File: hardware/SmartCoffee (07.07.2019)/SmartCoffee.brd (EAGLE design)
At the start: 96 x 40 mm, 32 parts, among them IC1 ULN2003V12DR, K1 G2R

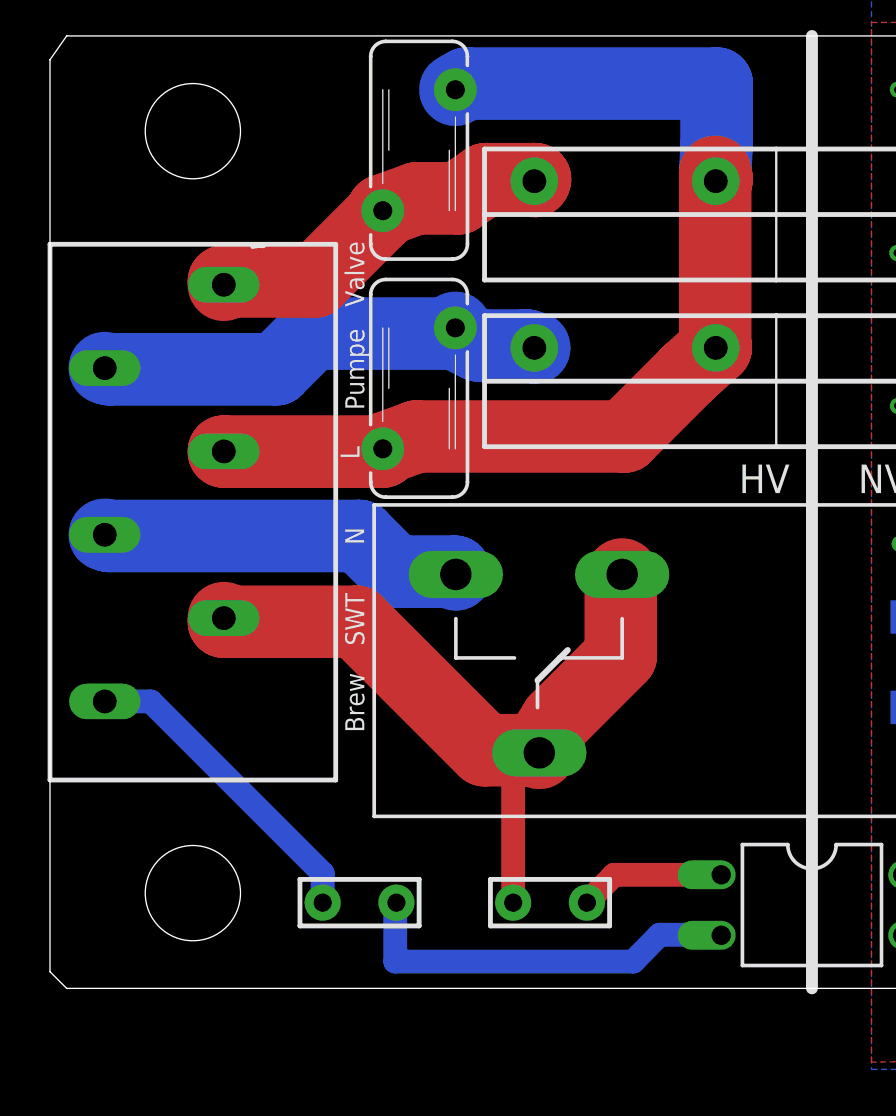
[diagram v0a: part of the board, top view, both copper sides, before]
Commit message: 
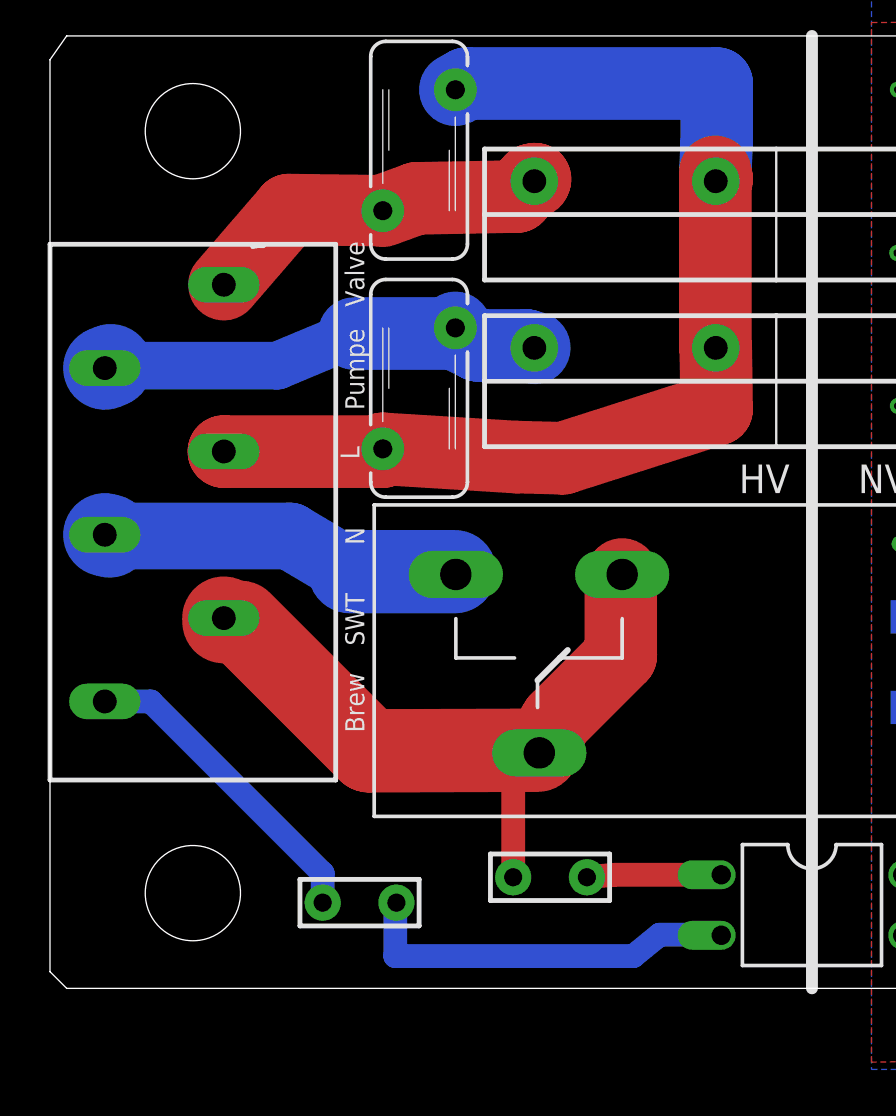
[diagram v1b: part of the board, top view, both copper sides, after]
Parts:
- moved R4 1.07 mm to (21.0, 4.67)
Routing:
- net HV_L: track 45.7 -> 47.0 mm
- net HV_N_SWITCHED: track 31.8 -> 30.8 mm
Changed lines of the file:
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@@
 <attribute name="VALUE" x="67.6506" y="39.3556" size="0.6" layer="122" font="vector" rot="MR180"/>
 </element>
-<element name="R4" library="myLib" package="RES_UPRIGHT" value="22k" x="21" y="3.6" smashed="yes" rot="R180"/>
+<element name="R4" library="myLib" package="RES_UPRIGHT" value="22k" x="21" y="4.6668" smashed="yes" rot="R180"/>
 <element name="R6" library="myLib" package="RES_UPRIGHT" value="22k" x="13" y="3.6" smashed="yes" rot="R180"/>
 <element name="LV_SUPPLY" library="con-pss254_reichelt" package="02G" value="" x="63.3114" y="40" rot="R180">
@@
 <wire x1="27.94" y1="26.9875" x2="27.96" y2="26.9" width="3.048" layer="1"/>
 <wire x1="27.94" y1="34.29" x2="27.96" y2="33.9" width="3.048" layer="16"/>
-<wire x1="24.13" y1="23.1775" x2="15.39875" y2="23.1775" width="3.048" layer="1"/>
-<wire x1="26.82875" y1="25.87625" x2="24.13" y2="23.1775" width="3.048" layer="1"/>
-<wire x1="15.39875" y1="23.1775" x2="13.976" y2="22.66" width="3.048" layer="1"/>
-<wire x1="26.82875" y1="25.87625" x2="27.96" y2="26.9" width="3.048" layer="1"/>
+<wire x1="21.5392" y1="22.2631" x2="19.56435" y2="22.3139" width="3.048" layer="1"/>
+<wire x1="27.99715" y1="24.32685" x2="21.5392" y2="22.2631" width="3.048" layer="1"/>
+<wire x1="19.56435" y1="22.3139" x2="13.976" y2="22.66" width="3.048" layer="1"/>
+<wire x1="27.99715" y1="24.32685" x2="27.96" y2="26.9" width="3.048" layer="1"/>
 <wire x1="28" y1="38" x2="17.5" y2="38" width="3.048" layer="16"/>
 <wire x1="28" y1="35.5" x2="28" y2="38" width="3.048" layer="16"/>
@@
 <contactref element="R4" pad="2"/>
 <contactref element="HV_SUPPLY" pad="L5"/>
-<wire x1="12.85875" y1="15.39875" x2="7.3025" y2="15.39875" width="3.048" layer="1"/>
-<wire x1="18.25625" y1="10.00125" x2="12.85875" y2="15.39875" width="3.048" layer="1"/>
-<wire x1="20.47875" y1="10.00125" x2="18.25625" y2="10.00125" width="3.048" layer="1"/>
-<wire x1="7.3025" y1="15.39875" x2="7.3" y2="15.55" width="3.048" layer="1"/>
+<wire x1="8.00735" y1="15.37335" x2="7.3025" y2="15.39875" width="3.048" layer="1"/>
+<wire x1="13.40485" y1="9.97585" x2="8.00735" y2="15.37335" width="3.5" layer="1"/>
+<wire x1="20.47875" y1="10.00125" x2="13.40485" y2="9.97585" width="3.5" layer="1"/>
+<wire x1="7.3025" y1="15.39875" x2="7.3" y2="15.55" width="3.5" layer="1"/>
 <wire x1="20.47875" y1="10.00125" x2="20.5502" y2="9.89" width="3.048" layer="1"/>
 <wire x1="23.97125" y1="13.97" x2="23.97125" y2="17.30375" width="3.048" layer="1"/>
@@
 <wire x1="21.2725" y1="11.27125" x2="20.47875" y2="10.00125" width="3.048" layer="1"/>
 <wire x1="20.5502" y1="9.89" x2="19.4525" y2="9.89" width="1" layer="1"/>
-<wire x1="19.4525" y1="9.89" x2="19.4525" y2="3.6" width="1" layer="1"/>
+<wire x1="19.4525" y1="9.89" x2="19.4525" y2="4.6668" width="1" layer="1"/>
 </signal>
 <signal name="HV-L_PUMP" class="2">
@@
 <contactref element="SUPPLY_SSR1" pad="1"/>
 <contactref element="HV_SUPPLY" pad="L2"/>
-<wire x1="9.5" y1="26" x2="2.5" y2="26" width="3.048" layer="16"/>
-<wire x1="11" y1="27.5" x2="9.5" y2="26" width="3.048" layer="16"/>
-<wire x1="17" y1="27.5" x2="11" y2="27.5" width="3.048" layer="16"/>
-<wire x1="2.5" y1="26" x2="2.3" y2="26.05" width="3.048" layer="16"/>
+<wire x1="9.5508" y1="26.1524" x2="2.5508" y2="26.1524" width="2" layer="16"/>
+<wire x1="12.778" y1="27.5" x2="9.5508" y2="26.1524" width="2" layer="16"/>
+<wire x1="17" y1="27.5" x2="12.778" y2="27.5" width="3.048" layer="16"/>
+<wire x1="2.5508" y1="26.1524" x2="2.3" y2="26.05" width="3.5" layer="16"/>
 <wire x1="17" y1="27.5" x2="17.024" y2="27.74" width="3.048" layer="16"/>
 <wire x1="18" y1="27" x2="20" y2="27" width="3.048" layer="16"/>
@@
 <contactref element="K1" pad="S"/>
 <contactref element="HV_SUPPLY" pad="L4"/>
-<wire x1="13" y1="19" x2="2.5" y2="19" width="3.048" layer="16"/>
-<wire x1="14.5" y1="17.5" x2="13" y2="19" width="3.048" layer="16"/>
-<wire x1="17" y1="17.5" x2="14.5" y2="17.5" width="3.048" layer="16"/>
-<wire x1="2.5" y1="19" x2="2.3" y2="19.05" width="3.048" layer="16"/>
+<wire x1="10.079" y1="19" x2="2.5" y2="19" width="2.8" layer="16"/>
+<wire x1="12.595" y1="17.5" x2="10.079" y2="19" width="2.8" layer="16"/>
+<wire x1="17" y1="17.5" x2="12.595" y2="17.5" width="3.5" layer="16"/>
+<wire x1="2.5" y1="19" x2="2.3" y2="19.05" width="3.5" layer="16"/>
 <wire x1="17" y1="17.5" x2="17.045" y2="17.383" width="3.048" layer="16"/>
 </signal>
@@
 <contactref element="SUPPLY_SSR2" pad="1"/>
 <contactref element="HV_SUPPLY" pad="L1"/>
-<wire x1="11.1125" y1="29.68625" x2="7.3025" y2="29.68625" width="3.048" layer="1"/>
-<wire x1="13.97" y1="32.54375" x2="11.1125" y2="29.68625" width="3.048" layer="1"/>
-<wire x1="7.3025" y1="29.68625" x2="7.3" y2="29.55" width="3.048" layer="1"/>
-<wire x1="13.97" y1="32.54375" x2="13.976" y2="32.66" width="3.048" layer="1"/>
-<wire x1="18.30705" y1="33.9852" x2="20.3708" y2="33.9852" width="3.048" layer="1"/>
-<wire x1="17.145" y1="33.17875" x2="18.30705" y2="33.9852" width="3.048" layer="1"/>
-<wire x1="15.39875" y1="33.17875" x2="17.145" y2="33.17875" width="3.048" layer="1"/>
+<wire x1="20.23745" y1="33.9598" x2="20.3708" y2="33.9852" width="3.048" layer="1"/>
+<wire x1="19.6088" y1="33.25495" x2="20.23745" y2="33.9598" width="3.048" layer="1"/>
+<wire x1="15.39875" y1="33.17875" x2="19.6088" y2="33.25495" width="3.048" layer="1"/>
 <wire x1="20.3708" y1="33.9852" x2="20.34" y2="33.9" width="3.048" layer="1"/>
 <wire x1="15.39875" y1="33.17875" x2="13.976" y2="32.66" width="3.048" layer="1"/>
+<wire x1="13.976" y1="32.66" x2="10.029" y2="32.7108" width="3" layer="1"/>
+<wire x1="10.029" y1="32.7108" x2="7.3" y2="29.55" width="3" layer="1"/>
 </signal>
 <signal name="N$2">
 <contactref element="R4" pad="1"/>
 <contactref element="OK1" pad="1"/>
-<wire x1="22.5475" y1="3.6" x2="23.6905" y2="4.77" width="1" layer="1"/>
+<wire x1="22.5475" y1="4.6668" x2="23.6905" y2="4.77" width="1" layer="1"/>
 <wire x1="23.6905" y1="4.77" x2="28.19" y2="4.77" width="1" layer="1"/>
 </signal>
@@
 <contactref element="OK1" pad="2"/>
 <wire x1="25.6016" y1="2.254" x2="27.9492" y2="2.254" width="1" layer="16"/>
-<wire x1="24.5" y1="1.127" x2="25.6016" y2="2.254" width="1" layer="16"/>
-<wire x1="14.5" y1="1.127" x2="24.5" y2="1.127" width="1" layer="16"/>
-<wire x1="14.5" y1="3.5" x2="14.5" y2="1.127" width="1" layer="16"/>
+<wire x1="24.5" y1="1.3556" x2="25.6016" y2="2.254" width="1" layer="16"/>
+<wire x1="14.5" y1="1.3556" x2="24.5" y2="1.3556" width="1" layer="16"/>
+<wire x1="14.5" y1="3.5" x2="14.5" y2="1.3556" width="1" layer="16"/>
 <wire x1="27.9492" y1="2.254" x2="28.19" y2="2.23" width="0.381" layer="16"/>
 <wire x1="14.5" y1="3.5" x2="14.5475" y2="3.6" width="0.381" layer="16"/>
